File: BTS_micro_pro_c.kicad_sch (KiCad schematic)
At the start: 11 parts, among them J2 I2C, J3 Analog, J6 Analog, J7 Digital, P1 USB_C_Plug_USB2.0, U1 ATmega32U4-A, U3 AMS1117-3.3, Y1 Crystal

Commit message: More progress.
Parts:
- added C1, C2: 22uF, symbol Device:C_Polarized
- added C3, C4: 22pF, symbol Device:C
- added C5: 1uF, symbol Device:C
- added D2: D, symbol Device:D
- added R2: 1M, symbol Device:R
- added R3: 10K, symbol Device:R
- F1: value Polyfuse -> 500mA Polyfuse
- R1: value R -> 330
- Y1: value Crystal -> 8Mhz Crystal
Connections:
- net +3.3V is gone; now on net VCC: U3.2 (VO)
- net GND: now also C1.2, C2.2, C3.1, C4.2, C5.2
- net RX: now also U1.20 (PD2)
- net TX: now also U1.21 (PD3)
- net UVCC: now also U1.2 (UVCC), U1.7 (VBUS)
- net VCC: now also U1.14 (VCC), U1.24 (AVCC), U1.34 (VCC), U1.44 (AVCC), C1.1, R3.1
- net at U3.3 (VI): now also C2.1, D2.1 (K); no longer F1.2
- net at Y1.1: now also U1.16 (XTAL2), C4.1, R2.1
- net at Y1.2: now also U1.17 (XTAL1), C3.2, R2.2
- net D+: now reaches P1.A6 (D+), U1.4 (D+)
- net D-: now reaches P1.A7 (D-), U1.3 (D-)
- net at U1.13 (~{RESET}): now also R3.2
- net at U1.6 (UCAP): now also C5.1
- new net: D2.2 (A), F1.2
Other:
- moved on the sheet: D1, F1, J2, J3, J6, J7, P1, R1, U1, U3, Y1

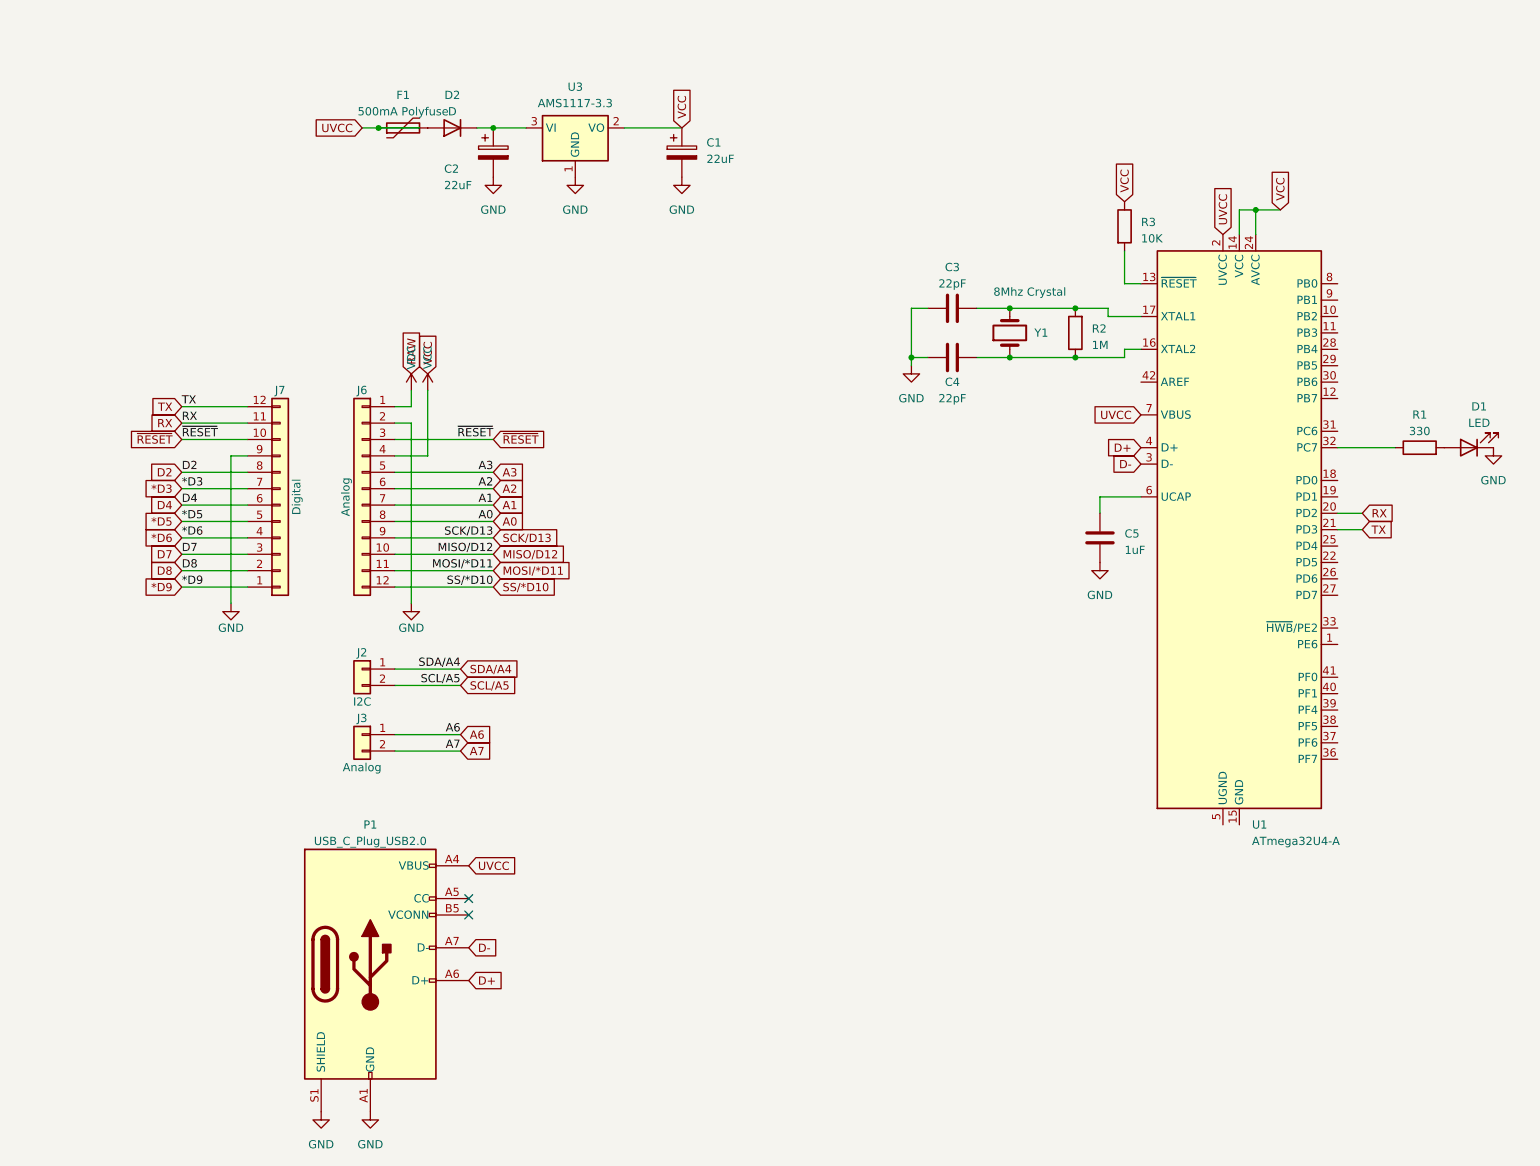
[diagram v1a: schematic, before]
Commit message: Schematic potentially done, needs footprints assigned though.
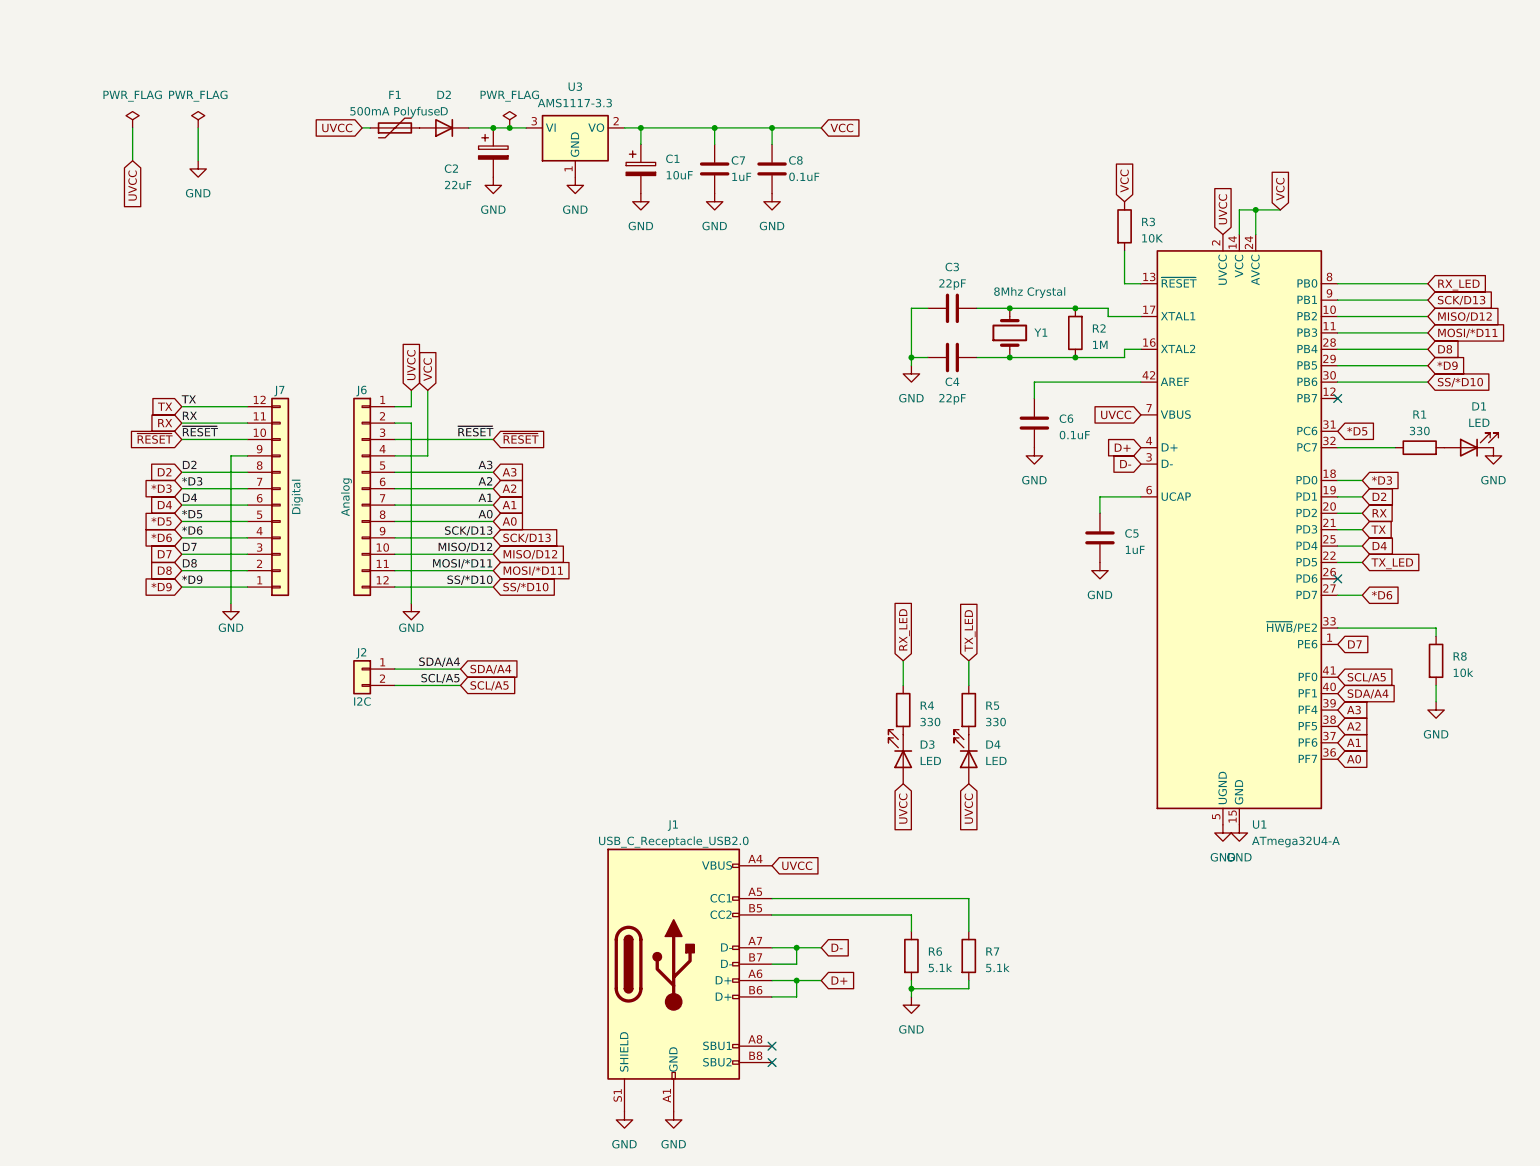
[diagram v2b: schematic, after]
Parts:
- removed J3: Analog, Connector_PinHeader_2.54mm:PinHeader_1x02_P2.54mm_Vertical, symbol Connector_Generic:Conn_01x02
- removed P1: USB_C_Plug_USB2.0, symbol Connector:USB_C_Plug_USB2.0
- added C6, C8: 0.1uF, Capacitor_SMD:C_0805_2012Metric_Pad1.18x1.45mm_HandSolder, symbol Device:C
- added C7: 1uF, Capacitor_SMD:C_0805_2012Metric_Pad1.18x1.45mm_HandSolder, symbol Device:C
- added D3, D4: LED, symbol Device:LED
- added J1: USB_C_Receptacle_USB2.0, symbol Connector:USB_C_Receptacle_USB2.0
- added R4, R5: 330, Resistor_SMD:R_0805_2012Metric_Pad1.20x1.40mm_HandSolder, symbol Device:R
- added R6, R7: 5.1k, Resistor_SMD:R_0805_2012Metric_Pad1.20x1.40mm_HandSolder, symbol Device:R
- added R8: 10k, Resistor_SMD:R_0805_2012Metric_Pad1.20x1.40mm_HandSolder, symbol Device:R
- C1: value 22uF -> 10uF; footprint (none) -> Capacitor_SMD:C_0805_2012Metric_Pad1.18x1.45mm_HandSolder
- C2, C3, C4, C5: footprint (none) -> Capacitor_SMD:C_0805_2012Metric_Pad1.18x1.45mm_HandSolder
- R1, R2, R3: footprint (none) -> Resistor_SMD:R_0805_2012Metric_Pad1.20x1.40mm_HandSolder
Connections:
- net VDC is gone; now on net UVCC: J6.1 (Pin_1)
- net *D3: now also U1.18 (PD0)
- net *D5: now also U1.31 (PC6)
- net *D6: now also U1.27 (PD7)
- net *D9: now also U1.29 (PB5)
- net A0: now also U1.36 (PF7)
- net A1: now also U1.37 (PF6)
- net A2: now also U1.38 (PF5)
- net A3: now also U1.39 (PF4)
- net D+: now also J1.A6 (D+), J1.B6 (D+)
- net D-: now also J1.A7 (D-), J1.B7 (D-)
- net D2: now also U1.19 (PD1)
- net D4: now also U1.25 (PD4)
- net D7: now also U1.1 (PE6)
- net D8: now also U1.28 (PB4)
- net GND: now also U1.15 (GND), U1.23 (GND), U1.35 (GND), U1.43 (GND), U1.5 (UGND), C6.2, C7.2, C8.2, J1.A1 (GND), J1.A12 (GND), J1.B1 (GND), J1.B12 (GND), J1.S1 (SHIELD), R6.2, R7.2, R8.2
- net MISO/D12: now also U1.10 (PB2)
- net MOSI/*D11: now also U1.11 (PB3)
- net SCK/D13: now also U1.9 (PB1)
- net SCL/A5: now also U1.41 (PF0)
- net SDA/A4: now also U1.40 (PF1)
- net SS/*D10: now also U1.30 (PB6)
- net UVCC: now also D3.2 (A), D4.2 (A), J1.A4 (VBUS), J1.A9 (VBUS), J1.B4 (VBUS), J1.B9 (VBUS)
- net VCC: now also C7.1, C8.1
- net TX_LED: now reaches U1.22 (PD5)
- net TX_LED: now also R5.1
- net at U1.33 (~{HWB}/PE2): now also R8.1
- net at U1.42 (AREF): now also C6.1
- net RX_LED: now reaches U1.8 (PB0)
- net RX_LED: now also R4.1
- new net: D3.1 (K), R4.2
- new net: D4.1 (K), R5.2
- new net: J1.A5 (CC1), R7.1
- new net: J1.B5 (CC2), R6.1
- no-connect marks 2 -> 4
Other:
- moved on the sheet: C1, D2, F1

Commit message: Finish rev1.
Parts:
- removed D3, D4: LED, symbol Device:LED
- removed J1: USB_C_Receptacle_USB2.0, symbol Connector:USB_C_Receptacle_USB2.0
- removed J2: I2C, Connector_PinHeader_2.54mm:PinHeader_1x02_P2.54mm_Vertical, symbol Connector_Generic:Conn_01x02
- removed R4, R5: 330, Resistor_SMD:R_0805_2012Metric_Pad1.20x1.40mm_HandSolder, symbol Device:R
- added J1: USB4105-GF-A, USB4105-GF-A:GCT_USB4105-GF-A, symbol USB4105-GF-A:USB4105-GF-A
- C1, C2, C3, C4, C5, C6, C7, C8: footprint Capacitor_SMD:C_0805_2012Metric_Pad1.18x1.45mm_HandSolder -> Capacitor_SMD:C_0402_1005Metric
- D1: footprint (none) -> LED_SMD:LED_0402_1005Metric
- D2: footprint (none) -> Diode_SMD:D_0402_1005Metric; LCSC (none) -> C316041
- F1: footprint (none) -> Fuse:Fuse_0805_2012Metric
- R1, R2, R3, R6, R7, R8: footprint Resistor_SMD:R_0805_2012Metric_Pad1.20x1.40mm_HandSolder -> Resistor_SMD:R_0402_1005Metric
- U1: footprint Package_QFP:TQFP-44_10x10mm_P0.8mm -> Package_DFN_QFN:QFN-44-1EP_7x7mm_P0.5mm_EP5.2x5.2mm; LCSC (none) -> C112161
- U3: footprint Package_TO_SOT_SMD:SOT-223-3_TabPin2 -> Package_TO_SOT_SMD:SOT-23-3; LCSC (none) -> C3015484
- Y1: footprint (none) -> Crystal:Crystal_SMD_3225-4Pin_3.2x2.5mm
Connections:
- net D+: now also J1.A6 (DP1), J1.B6 (DP2)
- net D-: now also J1.A7 (DN1), J1.B7 (DN2)
- net GND: now also J1.A1_B12 (GND), J1.B1_A12 (GND), J1.S1 (SHELL_GND), J1.S2 (SHELL_GND), J1.S3 (SHELL_GND), J1.S4 (SHELL_GND)
- net UVCC: now also J1.A4_B9 (VBUS), J1.B4_A9 (VBUS)
- net ~{RESET}: now also R3.2, U1.13 (~{RESET})
- net XTAL2: now reaches C4.1, R2.1, U1.16 (XTAL2), Y1.1
- net XTAL1: now reaches C3.2, R2.2, U1.17 (XTAL1), Y1.2
- net UCAP: now reaches C5.1, U1.6 (UCAP)
- net at R7.1: now also J1.B5 (CC2)
- net ~{HWB}/PE2: now reaches R8.1, U1.33 (~{HWB}/PE2)
- net at R6.1: now also J1.A5 (CC1)
- net RX_LED: no longer names the net of U1.8 (PB0)
- net SCL/A5: no longer names the net of U1.41 (PF0)
- net SDA/A4: no longer names the net of U1.40 (PF1)
- net TX_LED: no longer names the net of U1.22 (PD5)
- no-connect marks 4 -> 8

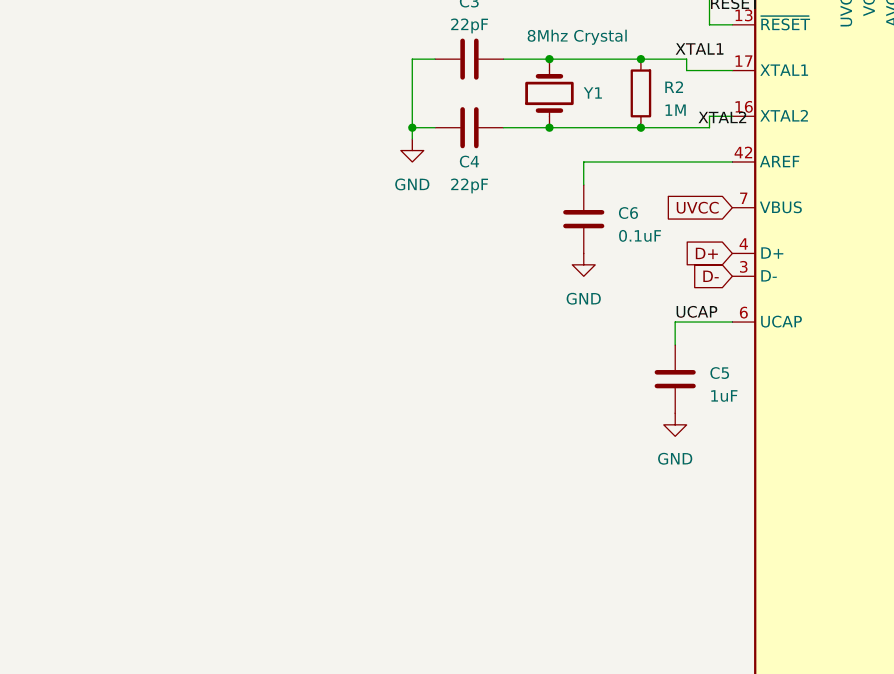
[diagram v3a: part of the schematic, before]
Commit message: Start rev 2.
In schematic, add USB resistors, put back I2C port.

Also, fix rotation issue that JLCPCB DFM picked up.
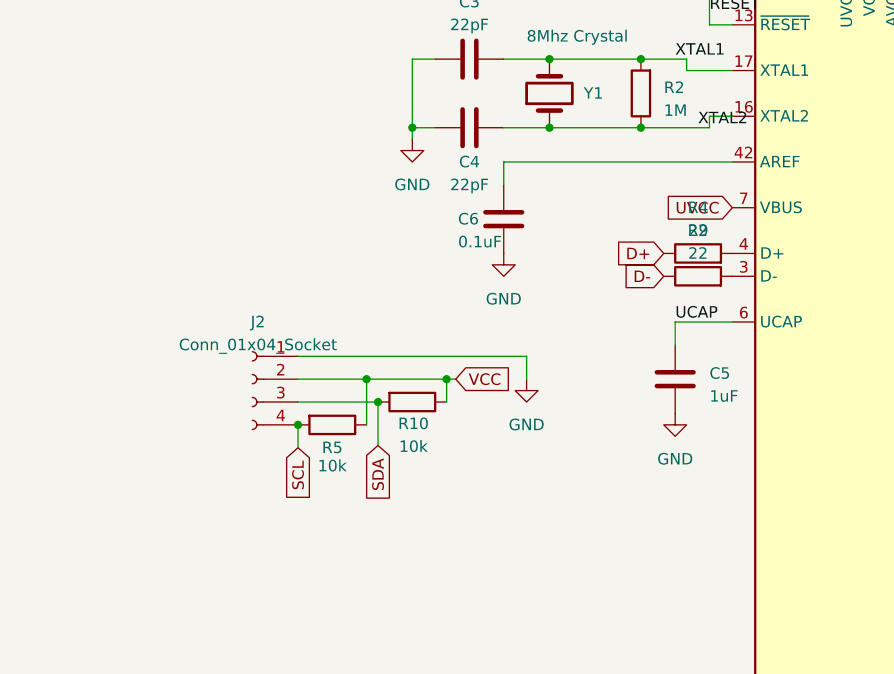
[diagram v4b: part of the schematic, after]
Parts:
- added J2: Conn_01x04_Socket, Connector_JST:JST_SH_SM04B-SRSS-TB_1x04-1MP_P1.00mm_Horizontal, symbol Connector:Conn_01x04_Socket
- added R10, R5: 10k, symbol Device:R
- added R4, R9: 22, symbol Device:R
- U1: JLCPCB Rotation Offset (none) -> -90
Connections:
- net D+: now also R4.1; no longer U1.4 (D+)
- net D-: now also R9.1; no longer U1.3 (D-)
- net GND: now also J2.1 (Pin_1)
- net VCC: now also J2.2 (Pin_2), R10.1, R5.1
- new net: R9.2, U1.3 (D-)
- new net: R4.2, U1.4 (D+)
- new net SCL: J2.4 (Pin_4), R5.2
- new net SDA: J2.3 (Pin_3), R10.2
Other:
- moved on the sheet: C6
